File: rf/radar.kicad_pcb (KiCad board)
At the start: 4 copper layers, 52 x 68 mm, 137 parts, among them J101 Conn_01x03, J102 Conn_Coaxial, J103 Conn_01x04, J104 Conn_01x03, J105 Conn_01x03, J106 Conn_Coaxial, J107 Conn_01x02, J801 Conn_01x02, T401 2450BL15B100, T402 2450BL15B050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

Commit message: Improve layout slightly
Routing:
- net GND: track 853.7 -> 855.2 mm
- net +12VA: track 83.7 -> 84.7 mm
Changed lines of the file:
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@@
     (thickness 1.6)
     (drawings 4)
-    (tracks 1796)
+    (tracks 1800)
     (zones 0)
     (modules 137)
@@
   )
   (setup
-    (last_trace_width 0.1524)
+    (last_trace_width 0.762)
     (user_trace_width 0.25)
     (user_trace_width 0.381)
@@
     (tags "capacitor 0603")
     (attr smd)
-    (fp_text reference C607 (at 0 -1.25 270) (layer F.SilkS)
+    (fp_text reference C607 (at -4.1021 0.1143 270) (layer F.SilkS)
       (effects (font (size 1 1) (thickness 0.15)))
     )
@@
     (tags "capacitor 0603")
     (attr smd)
-    (fp_text reference C501 (at -0.0675 1.2938) (layer F.SilkS)
+    (fp_text reference C501 (at 1.5977 -1.4732) (layer F.SilkS)
       (effects (font (size 1 1) (thickness 0.15)))
     )
@@
     (tags "capacitor 0402")
     (attr smd)
-    (fp_text reference C502 (at 1.7867 -1.3924 180) (layer F.SilkS)
+    (fp_text reference C502 (at -0.4445 -1.8415 360) (layer F.SilkS)
       (effects (font (size 1 1) (thickness 0.15)))
     )
@@
     (tags "capacitor 0603")
     (attr smd)
-    (fp_text reference C503 (at -0.1143 1.3597) (layer F.SilkS)
+    (fp_text reference C503 (at 1.7018 1.5367) (layer F.SilkS)
       (effects (font (size 1 1) (thickness 0.15)))
     )
@@
     (tags "capacitor 0402")
     (attr smd)
-    (fp_text reference C504 (at -1.3383 -1.0011 180) (layer F.SilkS)
+    (fp_text reference C504 (at -0.7151 -1.9304 180) (layer F.SilkS)
       (effects (font (size 1 1) (thickness 0.15)))
     )
@@
     (tags "capacitor 0603")
     (attr smd)
-    (fp_text reference C601 (at -0.2308 1.3285 270) (layer F.SilkS)
+    (fp_text reference C601 (at -0.1778 -1.4478 270) (layer F.SilkS)
       (effects (font (size 1 1) (thickness 0.15)))
     )
@@
     (tags "capacitor 0603")
     (attr smd)
-    (fp_text reference C602 (at -3.7622 -0.2955 90) (layer F.SilkS)
+    (fp_text reference C602 (at -2.7788 -0.2413 180) (layer F.SilkS)
       (effects (font (size 1 1) (thickness 0.15)))
     )
@@
     (tags "capacitor 0603")
     (attr smd)
-    (fp_text reference C603 (at -3.7487 0.0051 90) (layer F.SilkS)
+    (fp_text reference C603 (at 0.2057 1.4986 90) (layer F.SilkS)
       (effects (font (size 1 1) (thickness 0.15)))
     )
@@
     (tags "capacitor 0402")
     (attr smd)
-    (fp_text reference L501 (at 0.2559 -2.1993 270) (layer F.SilkS)
+    (fp_text reference L501 (at -0.3283 1.2297 360) (layer F.SilkS)
       (effects (font (size 1 1) (thickness 0.15)))
     )
@@
     (tags "resistor 0402")
     (attr smd)
-    (fp_text reference R603 (at 0 -1.35) (layer F.SilkS)
+    (fp_text reference R603 (at -0.0381 -2.5273 90) (layer F.SilkS)
       (effects (font (size 1 1) (thickness 0.15)))
     )
@@
     (tags "resistor 0603")
     (attr smd)
-    (fp_text reference R606 (at 0 -1.45 90) (layer F.SilkS)
+    (fp_text reference R606 (at -3.9448 -0.0254 90) (layer F.SilkS)
       (effects (font (size 1 1) (thickness 0.15)))
     )
@@
     (tags "resistor 0603")
     (attr smd)
-    (fp_text reference R607 (at 0 -1.45 90) (layer F.SilkS)
+    (fp_text reference R607 (at 3.7465 0.0762 90) (layer F.SilkS)
       (effects (font (size 1 1) (thickness 0.15)))
     )
@@
     (tags "resistor 0603")
     (attr smd)
-    (fp_text reference R611 (at 0 -1.45 90) (layer F.SilkS)
+    (fp_text reference R611 (at 3.9624 -0.1778 90) (layer F.SilkS)
       (effects (font (size 1 1) (thickness 0.15)))
     )
@@
     (tags "resistor 0603")
     (attr smd)
-    (fp_text reference R612 (at 0 -1.45 90) (layer F.SilkS)
+    (fp_text reference R612 (at 4.0689 -0.0889 90) (layer F.SilkS)
       (effects (font (size 1 1) (thickness 0.15)))
     )
@@
     (tags "resistor 0402")
     (attr smd)
-    (fp_text reference R613 (at 0 -1.35 180) (layer F.SilkS)
+    (fp_text reference R613 (at 0.0635 2.4384 270) (layer F.SilkS)
       (effects (font (size 1 1) (thickness 0.15)))
     )
@@
     (tags "resistor 0603")
     (attr smd)
-    (fp_text reference R614 (at 0 -1.45 270) (layer F.SilkS)
+    (fp_text reference R614 (at -4.1021 0.2794 270) (layer F.SilkS)
       (effects (font (size 1 1) (thickness 0.15)))
     )
@@
   (gr_line (start 152 100) (end 152 168) (layer Edge.Cuts) (width 0.15))
   (gr_line (start 100 100) (end 152 100) (layer Edge.Cuts) (width 0.15))
+  (segment (start 111.25 134.9) (end 113.35 132.8) (width 0.762) (layer In1.Cu) (net 1))
+  (segment (start 113.35 132.8) (end 113.338 132.8) (width 0.762) (layer In1.Cu) (net 1))
+  (segment (start 113.338 132.8) (end 113.3 132.762) (width 0.762) (layer In1.Cu) (net 1))
+  (segment (start 113.3 132.762) (end 113.3 131.4) (width 0.762) (layer In1.Cu) (net 1))
+  (via (at 113.3 131.4) (size 0.6858) (drill 0.3302) (layers F.Cu B.Cu) (net 1))
   (segment (start 143.0489 152.146) (end 143.004 152.146) (width 0.4) (layer F.Cu) (net 1))
   (segment (start 143.004 152.146) (end 142.6 152.55) (width 0.4) (layer F.Cu) (net 1))
@@
   (segment (start 113.465067 135.75) (end 113.5 135.75) (width 0.762) (layer In1.Cu) (net 1))
   (segment (start 110.4 135.75) (end 111.25 134.9) (width 0.762) (layer In1.Cu) (net 1))
-  (segment (start 111.25 134.9) (end 111.55 134.6) (width 0.762) (layer In1.Cu) (net 1))
   (segment (start 129.265406 133.456934) (end 128.780473 133.456934) (width 0.762) (layer In1.Cu) (net 1))
   (segment (start 128.29554 133.456934) (end 128.780473 133.456934) (width 0.381) (layer In1.Cu) (net 1))
@@
   (segment (start 118.65 143.75) (end 118.65 142.7) (width 0.381) (layer B.Cu) (net 1))
   (via (at 118.65 142.7) (size 0.6858) (drill 0.3302) (layers F.Cu B.Cu) (net 1))
-  (segment (start 111.55 134.6) (end 113.35 132.8) (width 0.762) (layer In1.Cu) (net 1))
   (segment (start 109.06071 140.6) (end 109.06071 137.08929) (width 0.762) (layer In1.Cu) (net 1))
   (segment (start 106.2 160.53137) (end 106.2 159.2) (width 0.762) (layer In1.Cu) (net 1))
@@
   (via (at 133.85 118.3) (size 0.6858) (drill 0.3302) (layers F.Cu B.Cu) (net 1))
   (via (at 120.45 146.2) (size 0.6858) (drill 0.3302) (layers F.Cu B.Cu) (net 1))
-  (via (at 113.35 132.8) (size 0.6858) (drill 0.3302) (layers F.Cu B.Cu) (net 1))
   (via (at 102.24051 138.9) (size 0.6858) (drill 0.3302) (layers F.Cu B.Cu) (net 1))
   (via (at 132.35 117.75) (size 0.6858) (drill 0.3302) (layers F.Cu B.Cu) (net 1))
@@
   (segment (start 123.3 141) (end 124 140.3) (width 0.762) (layer B.Cu) (net 23))
   (segment (start 118.95 141) (end 120 141) (width 0.762) (layer B.Cu) (net 23))
+  (segment (start 115.2 133.05) (end 115.2 133.15) (width 0.762) (layer In2.Cu) (net 24))
+  (segment (start 115.2 133.15) (end 114.55 133.8) (width 0.762) (layer In2.Cu) (net 24))
   (via (at 114.2 144.5) (size 0.6858) (drill 0.3302) (layers F.Cu B.Cu) (net 24))
   (segment (start 103.7 154.357101) (end 102.642899 154.357101) (width 0.762) (layer In2.Cu) (net 24))
@@
     (polygon
       (pts
-        (xy 102 157.8) (xy 102 161) (xy 110.2 161) (xy 114 157.2) (xy 114 146.2)
-        (xy 115 145.2) (xy 115 134) (xy 115 132.6) (xy 112.6 132.6) (xy 109.6 135.6)
+        (xy 102 157.8) (xy 102 161) (xy 110.2 161) (xy 114 157.2) (xy 114.9858 156.1973)
+        (xy 115 145.2) (xy 115 134) (xy 115 132.6) (xy 109.601 132.6515) (xy 109.6 135.6)
         (xy 109.6 144.8) (xy 102 152.8)
       )

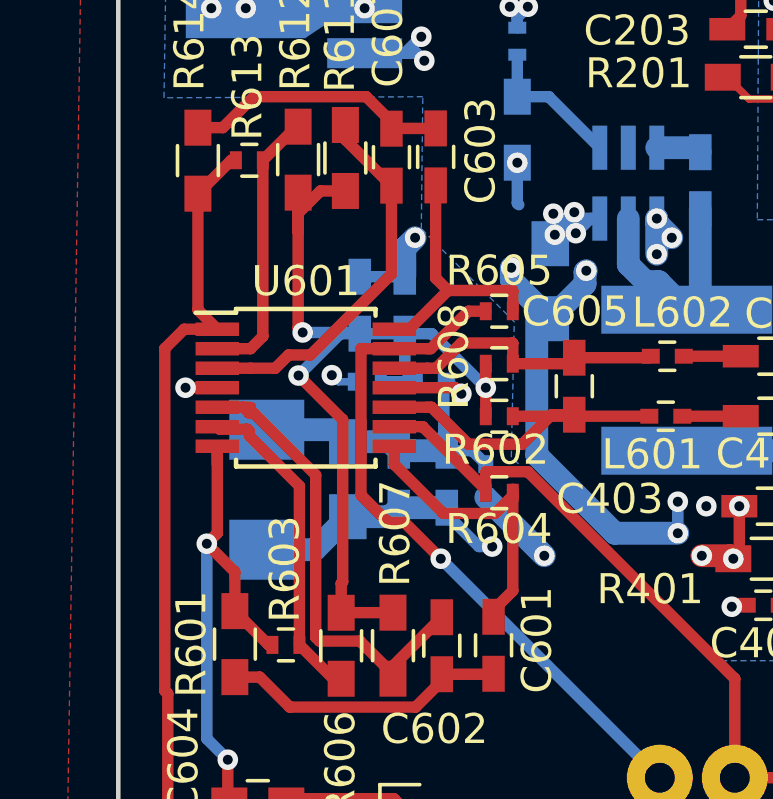
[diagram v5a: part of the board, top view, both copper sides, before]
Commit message: Fix voltage rails on op amp
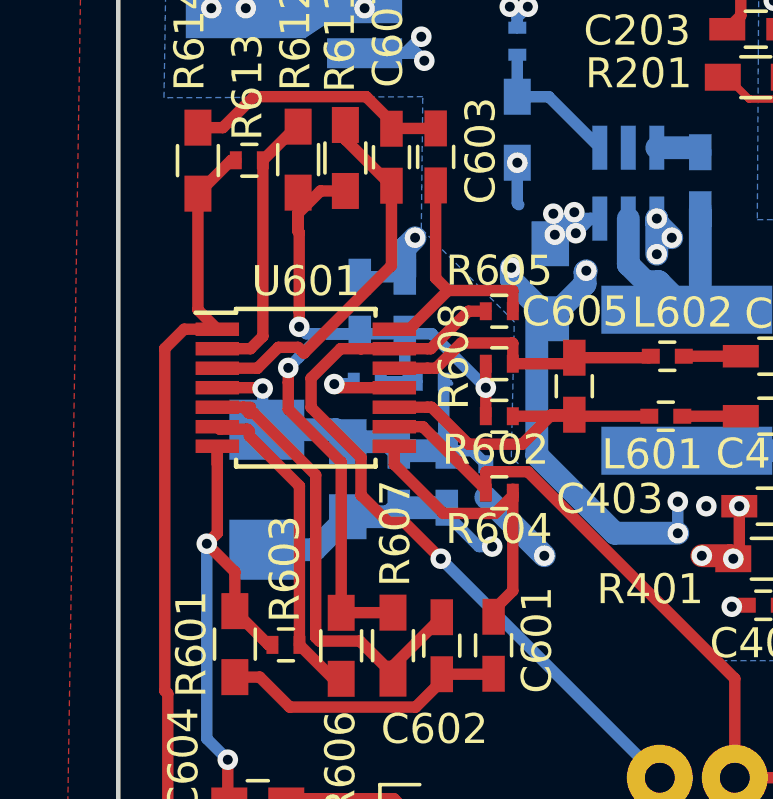
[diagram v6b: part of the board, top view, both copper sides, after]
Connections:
- U601 pad 11: +12V -> GND
- U601 pad 4: GND -> +12V
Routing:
- net GND: track 855.2 -> 847.9 mm, vias 180 -> 179
- net Net-(R605-Pad1): track 23.4 -> 25.2 mm
- net +6V: track 31.8 -> 32.4 mm

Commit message: Line up connectors across both boards, spread out component footprints
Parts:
- J101: value Conn_01x03 -> VCO_INTERFACE
- J103: value Conn_01x04 -> PLL_INTERFACE
- J104: value Conn_01x03 -> PA_INTERFACE
- J105: value Conn_01x03 -> LNA_INTERFACE
- J107: value Conn_01x02 -> BASEBAND
- J801: value Conn_01x02 -> RF_POWER
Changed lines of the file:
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@@
   )
   (setup
-    (last_trace_width 0.381)
+    (last_trace_width 0.1524)
     (user_trace_width 0.25)
     (user_trace_width 0.381)
@@
       (effects (font (size 1 1) (thickness 0.15)))
     )
-    (fp_text value Conn_01x04 (at 0 9.95) (layer F.Fab)
+    (fp_text value PLL_INTERFACE (at 0 9.95) (layer F.Fab)
       (effects (font (size 1 1) (thickness 0.15)))
     )
@@
       (effects (font (size 1 1) (thickness 0.15)))
     )
-    (fp_text value Conn_01x02 (at 0 4.87) (layer F.Fab)
+    (fp_text value BASEBAND (at 0 4.87) (layer F.Fab)
       (effects (font (size 1 1) (thickness 0.15)))
     )
@@
       (effects (font (size 1 1) (thickness 0.15)))
     )
-    (fp_text value Conn_01x02 (at 0 4.87) (layer F.Fab)
+    (fp_text value RF_POWER (at 0 4.87) (layer F.Fab)
       (effects (font (size 1 1) (thickness 0.15)))
     )
@@
       (effects (font (size 1 1) (thickness 0.15)))
     )
-    (fp_text value Conn_01x03 (at 0 7.41) (layer F.Fab)
+    (fp_text value VCO_INTERFACE (at 0 7.41) (layer F.Fab)
       (effects (font (size 1 1) (thickness 0.15)))
     )
@@
       (effects (font (size 1 1) (thickness 0.15)))
     )
-    (fp_text value Conn_01x03 (at 0 7.41) (layer F.Fab)
+    (fp_text value PA_INTERFACE (at 0 7.41) (layer F.Fab)
       (effects (font (size 1 1) (thickness 0.15)))
     )
@@
       (effects (font (size 1 1) (thickness 0.15)))
     )
-    (fp_text value Conn_01x03 (at 0 7.41 180) (layer F.Fab)
+    (fp_text value LNA_INTERFACE (at 0 7.41 180) (layer F.Fab)
       (effects (font (size 1 1) (thickness 0.15)))
     )

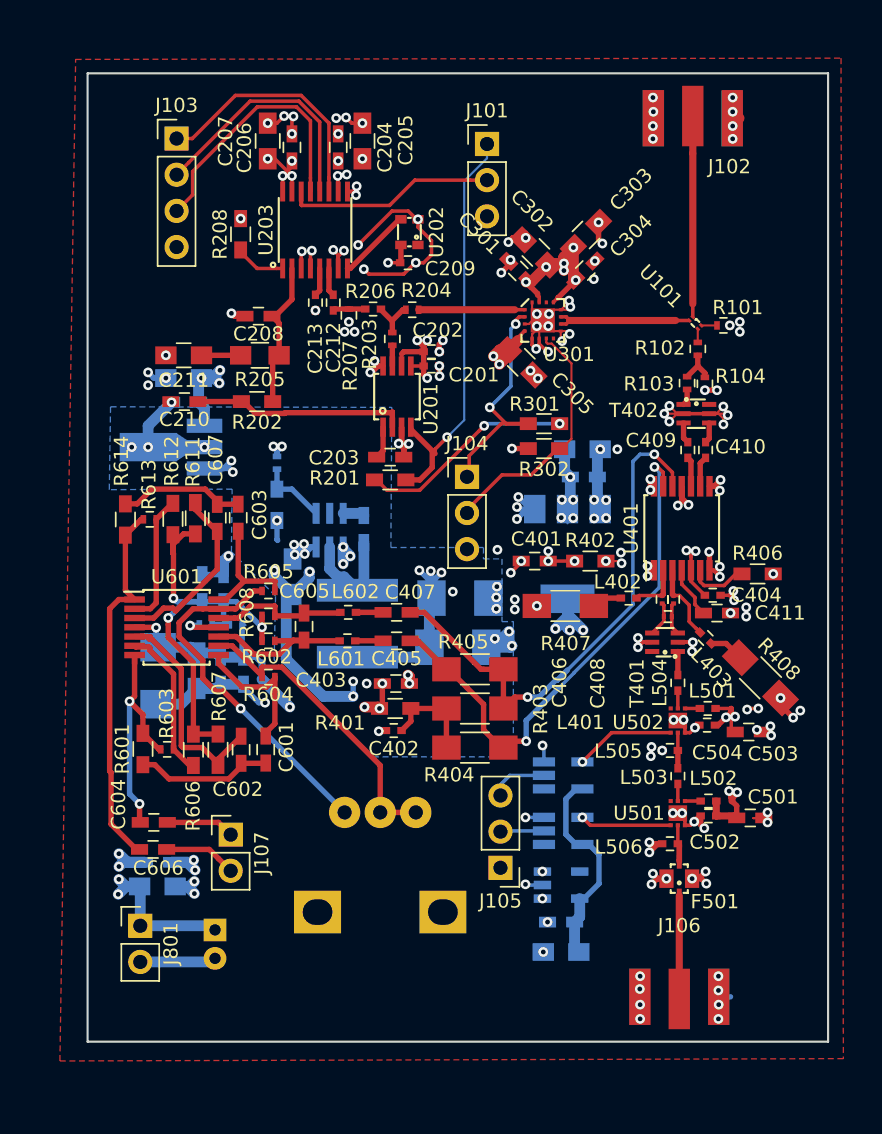
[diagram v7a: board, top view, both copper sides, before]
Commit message: Add via stitching to RF board
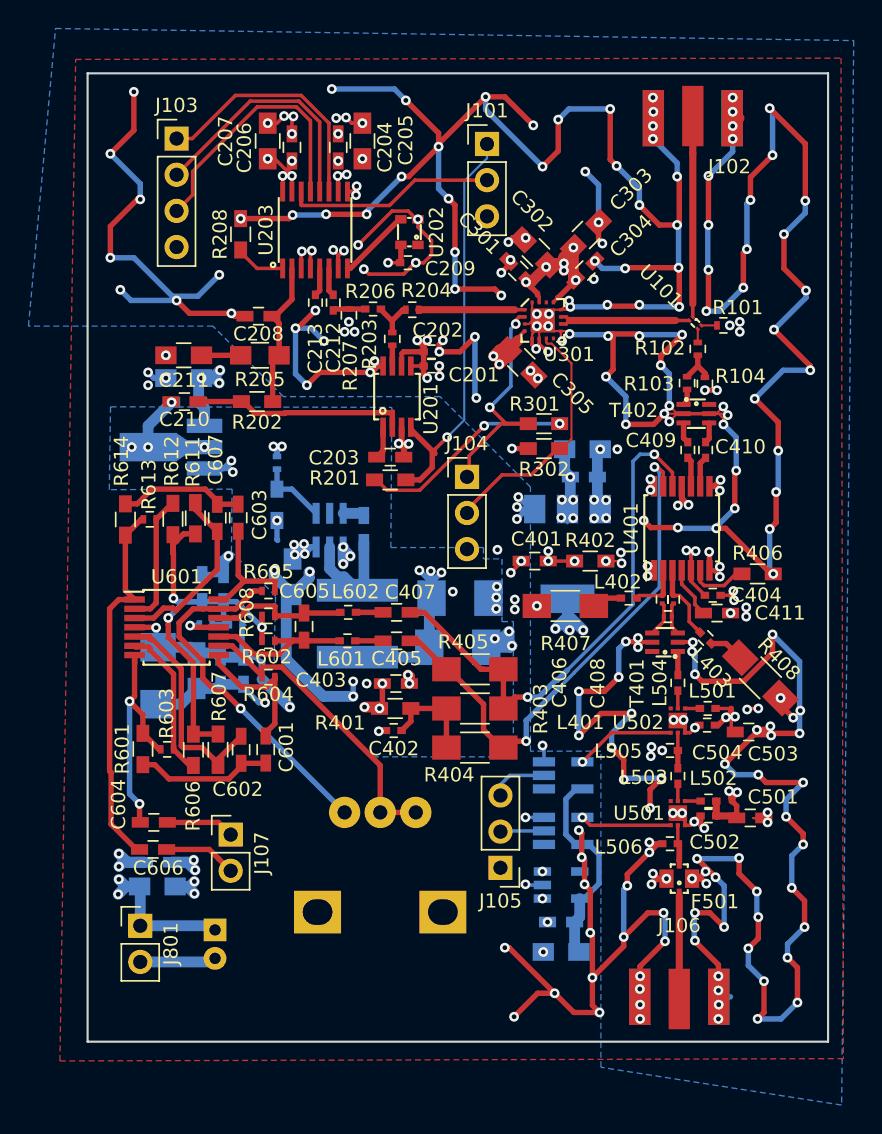
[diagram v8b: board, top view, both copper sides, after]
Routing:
- net GND: track 847.9 -> 1268.0 mm, vias 179 -> 291
- net +3V3: track 239.7 -> 238.5 mm
